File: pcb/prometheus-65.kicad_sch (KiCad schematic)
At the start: 0 parts

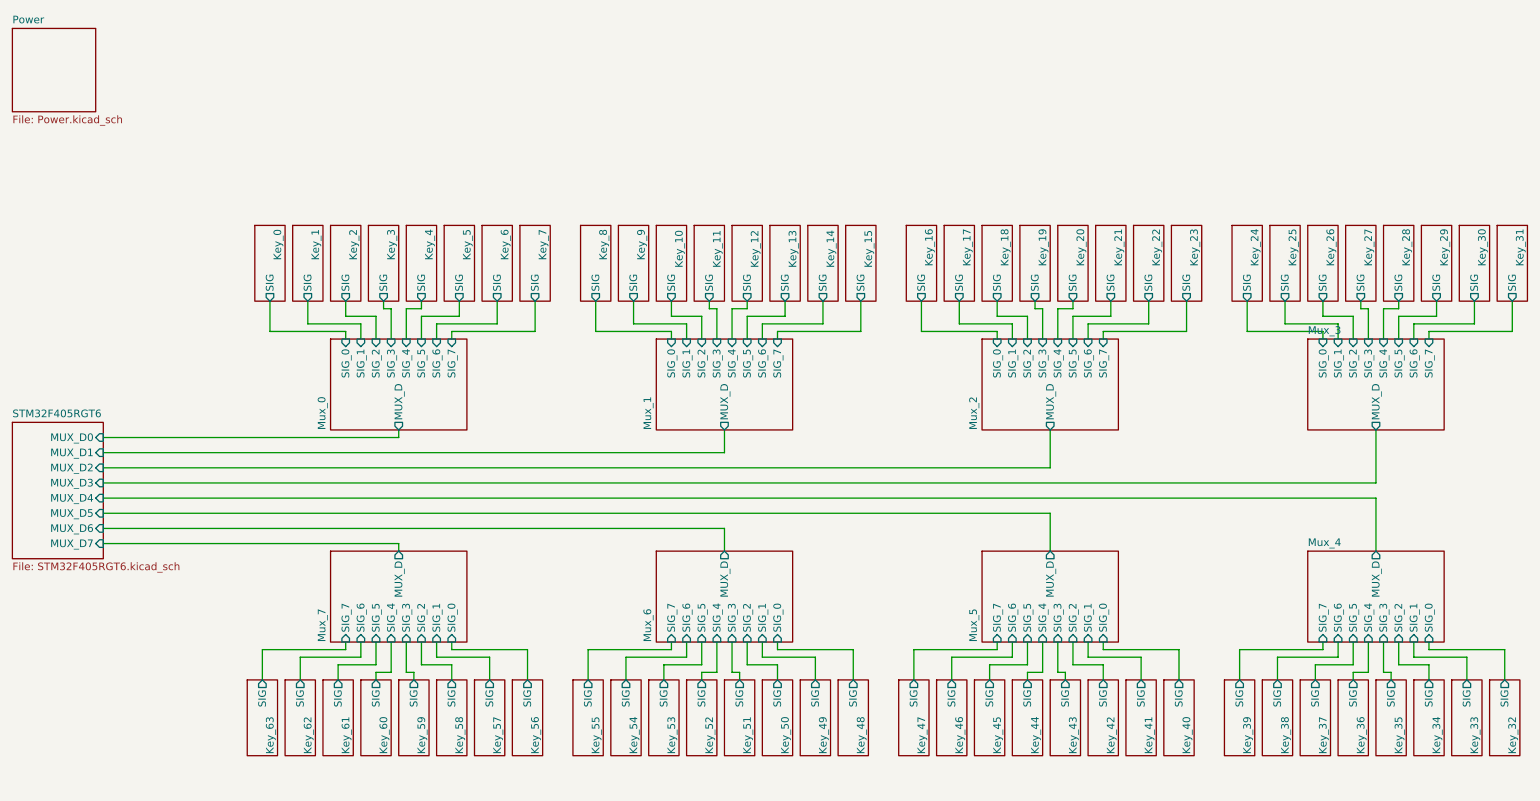
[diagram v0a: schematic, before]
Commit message: feat: added the rotary encoder
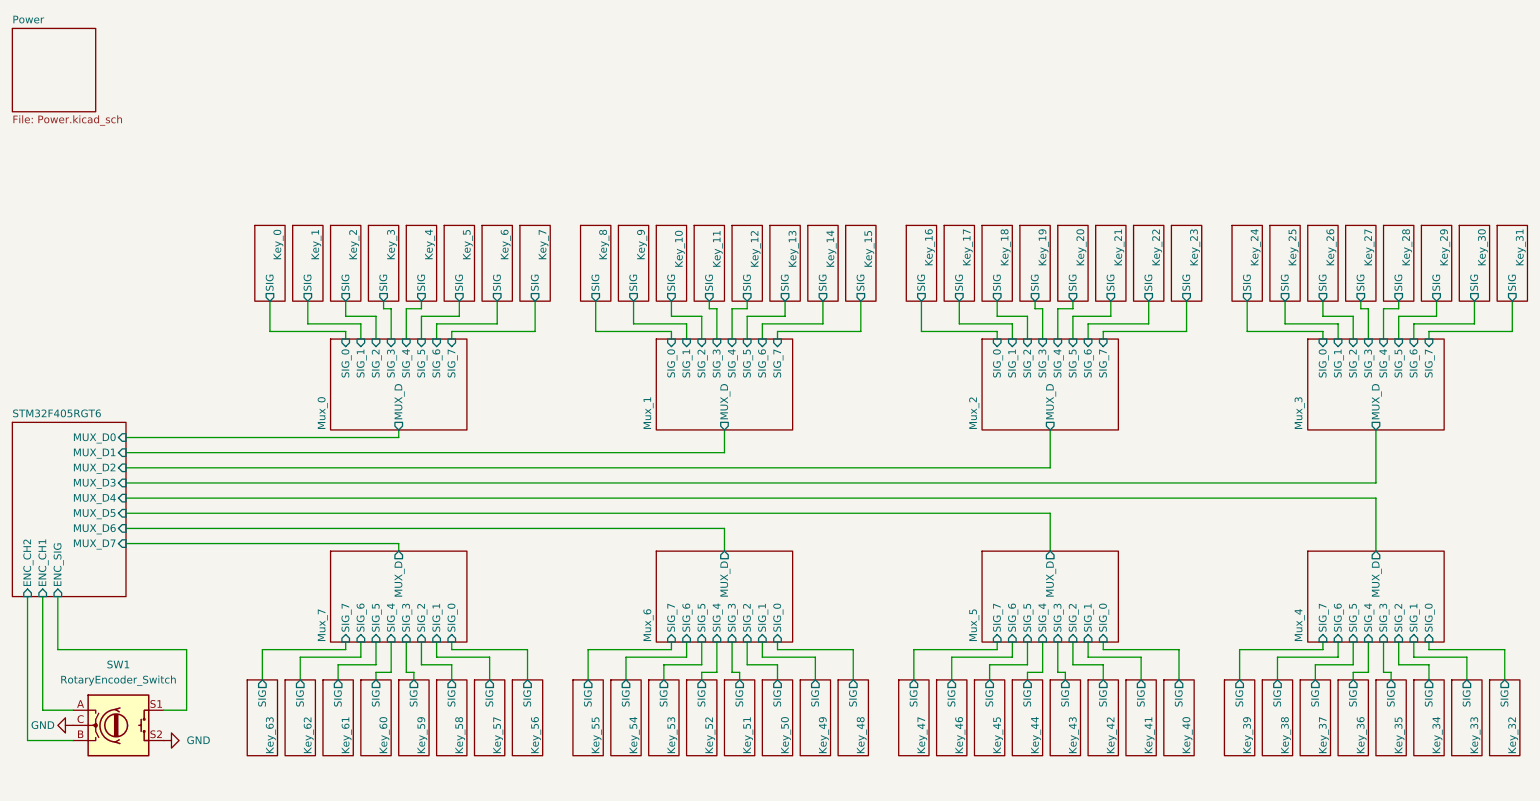
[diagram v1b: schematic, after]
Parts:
- added SW1: RotaryEncoder_Switch, symbol Device:RotaryEncoder_Switch
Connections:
- new net GND: SW1.C, SW1.S2
- new net STM32F405RGT6/ENC_CH1: SW1.A
- new net STM32F405RGT6/ENC_CH2: SW1.B
- new net STM32F405RGT6/ENC_SIG: SW1.S1
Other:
- sheet STM32F405RGT6 ports: added ENC_CH1, ENC_CH2, ENC_SIG; removed none

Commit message: feat: added LED circuit and wired to STM32
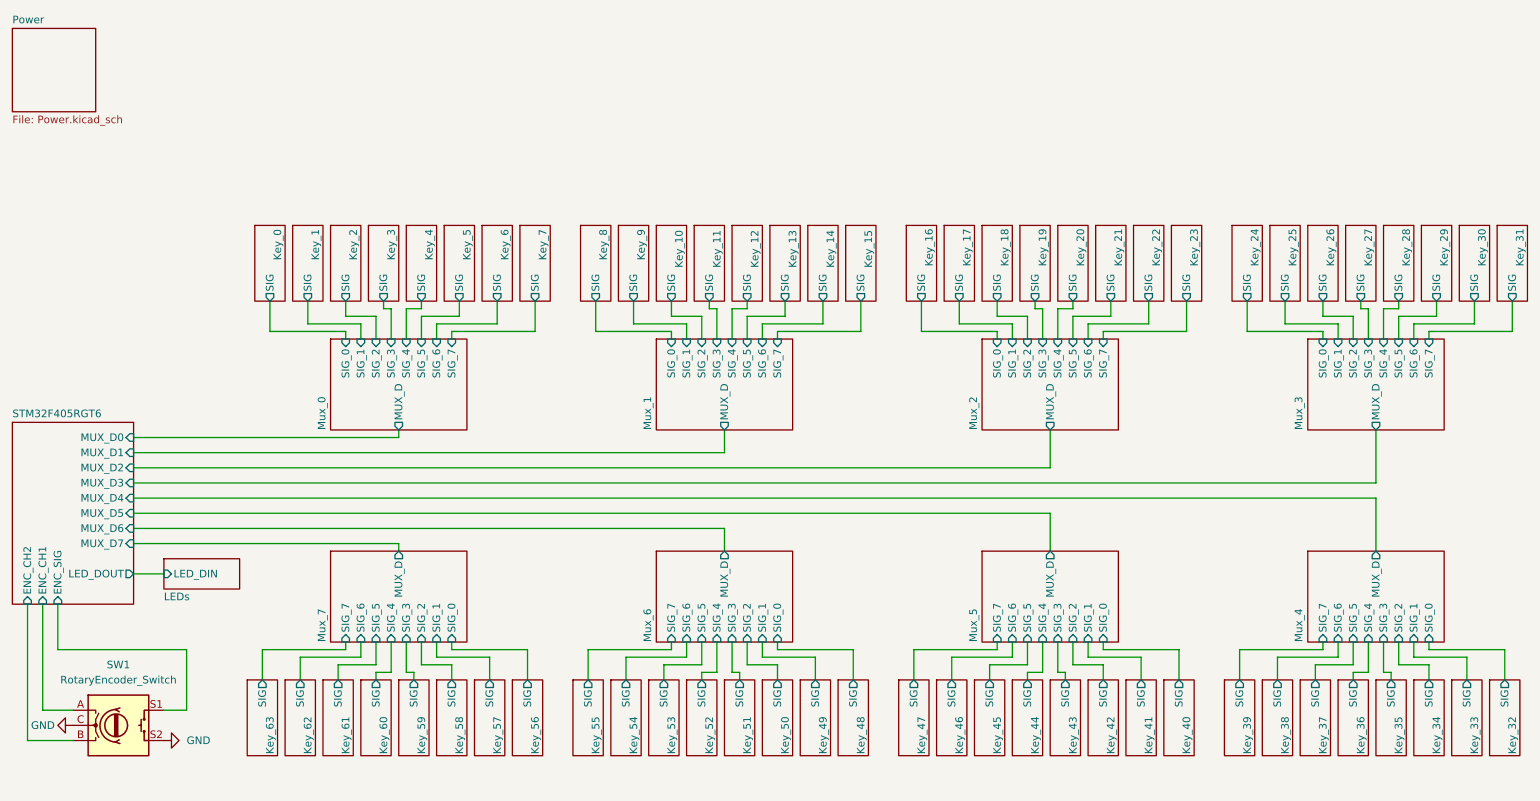
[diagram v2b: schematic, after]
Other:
- added sheet LEDs (LEDs.kicad_sch)
- sheet STM32F405RGT6 ports: added LED_DOUT; removed none

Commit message: feat: assigned footprints for each symbol and switch
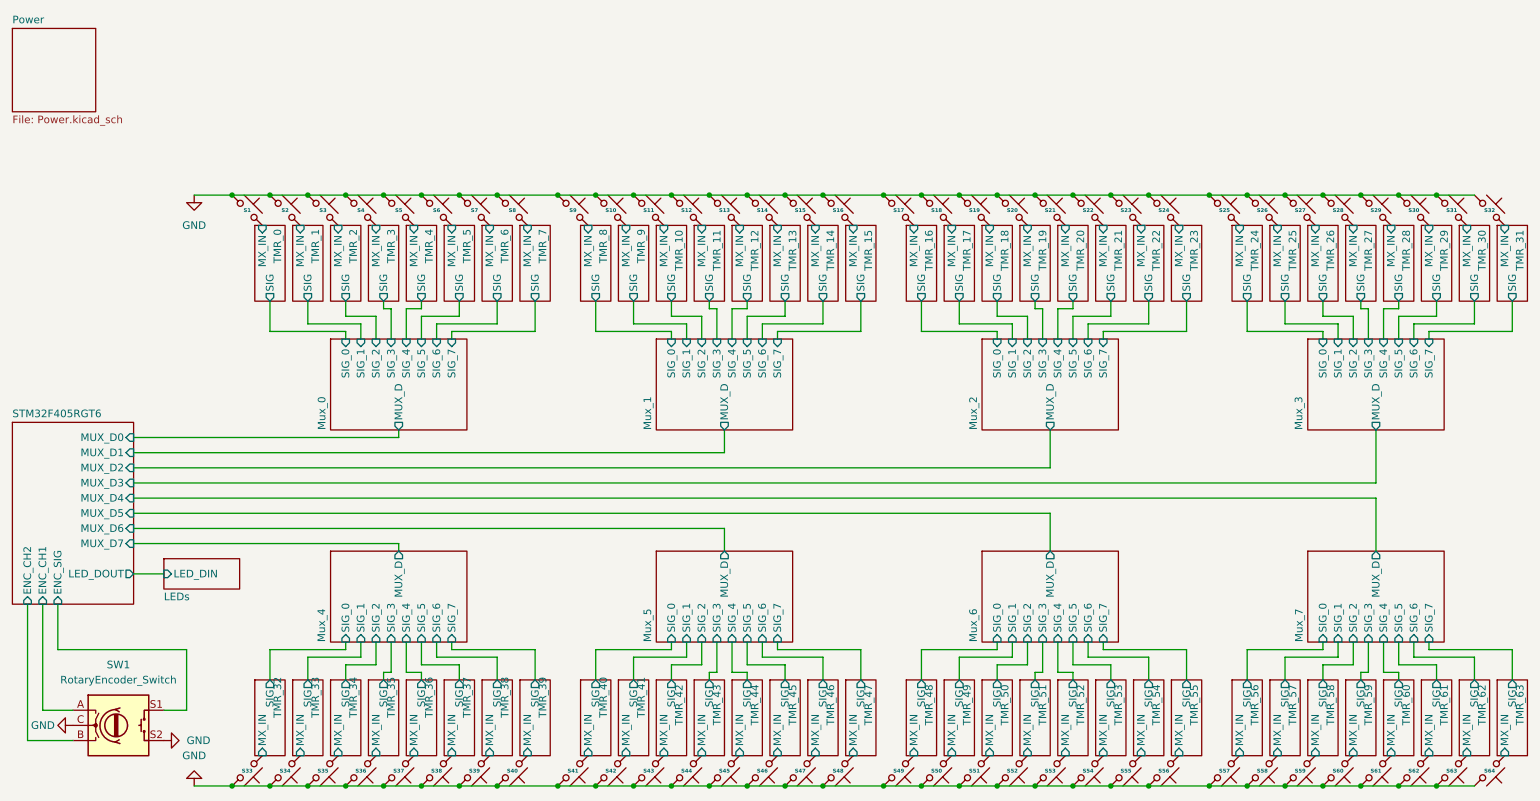
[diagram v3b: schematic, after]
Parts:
- added S1, S10, S12, S13, S17, S18, S19, S2, S20, S21, S22, S23, S24, S25, S26, S27, S28, S29, S3, S30, S31, S33, S34, S35, S36, S37, S38, S39, S4, S40, S41, S42, S43, S44, S45, S46, S47, S49, S50, S51, S53, S54, S55, S58, S6, S60, S64, S7, S9: ~, ScottoKeebs_Hotswap:Hotswap_MX_Plated_1.00u, symbol ScottoKeebs:Placeholder_Keyswitch
- added S11, S57: ~, ScottoKeebs_Hotswap:Hotswap_MX_Plated_2.25u, symbol ScottoKeebs:Placeholder_Keyswitch
- added S14, S15, S16, S48, S61, S62, S63: ~, ScottoKeebs_Hotswap:Hotswap_MX_Plated_1.25u, symbol ScottoKeebs:Placeholder_Keyswitch
- added S32: ~, ScottoKeebs_Hotswap:Hotswap_MX_Plated_6.25u, symbol ScottoKeebs:Placeholder_Keyswitch
- added S5, S56: ~, ScottoKeebs_Hotswap:Hotswap_MX_Plated_1.50u, symbol ScottoKeebs:Placeholder_Keyswitch
- added S52: ~, ScottoKeebs_Hotswap:Hotswap_MX_Plated_2.00u, symbol ScottoKeebs:Placeholder_Keyswitch
- added S59: ~, ScottoKeebs_Hotswap:Hotswap_MX_Plated_2.75u, symbol ScottoKeebs:Placeholder_Keyswitch
- added S8: ~, ScottoKeebs_Hotswap:Hotswap_MX_Plated_1.75u, symbol ScottoKeebs:Placeholder_Keyswitch
- SW1: footprint (none) -> Rotary_Encoder:RotaryEncoder_Alps_EC11E-Switch_Vertical_H20mm
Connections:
- net GND: now also S1.1, S10.1, S11.1, S12.1, S13.1, S14.1, S15.1, S16.1, S17.1, S18.1, S19.1, S2.1, S20.1, S21.1, S22.1, S23.1, S24.1, S25.1, S26.1, S27.1, S28.1, S29.1, S3.1, S30.1, S31.1, S32.1, S33.1, S34.1, S35.1, S36.1, S37.1, S38.1, S39.1, S4.1, S40.1, S41.1, S42.1, S43.1, S44.1, S45.1, S46.1, S47.1, S48.1, S49.1, S5.1, S50.1, S51.1, S52.1, S53.1, S54.1, S55.1, S56.1, S57.1, S58.1, S59.1, S6.1, S60.1, S61.1, S62.1, S63.1, S64.1, S7.1, S8.1, S9.1
- new net TMR_0/MX_IN: S1.2
- new net TMR_1/MX_IN: S2.2
- new net TMR_10/MX_IN: S11.2
- new net TMR_11/MX_IN: S12.2
- new net TMR_12/MX_IN: S13.2
- new net TMR_13/MX_IN: S14.2
- new net TMR_14/MX_IN: S15.2
- new net TMR_15/MX_IN: S16.2
- new net TMR_16/MX_IN: S17.2
- new net TMR_17/MX_IN: S18.2
- new net TMR_18/MX_IN: S19.2
- new net TMR_19/MX_IN: S20.2
- new net TMR_2/MX_IN: S3.2
- new net TMR_20/MX_IN: S21.2
- new net TMR_21/MX_IN: S22.2
- new net TMR_22/MX_IN: S23.2
- new net TMR_23/MX_IN: S24.2
- new net TMR_24/MX_IN: S25.2
- new net TMR_25/MX_IN: S26.2
- new net TMR_26/MX_IN: S27.2
- new net TMR_27/MX_IN: S28.2
- new net TMR_28/MX_IN: S29.2
- new net TMR_29/MX_IN: S30.2
- new net TMR_3/MX_IN: S4.2
- new net TMR_30/MX_IN: S31.2
- new net TMR_31/MX_IN: S32.2
- new net TMR_32/MX_IN: S33.2
- new net TMR_33/MX_IN: S34.2
- new net TMR_34/MX_IN: S35.2
- new net TMR_35/MX_IN: S36.2
- new net TMR_36/MX_IN: S37.2
- new net TMR_37/MX_IN: S38.2
- new net TMR_38/MX_IN: S39.2
- new net TMR_39/MX_IN: S40.2
- new net TMR_4/MX_IN: S5.2
- new net TMR_40/MX_IN: S41.2
- new net TMR_41/MX_IN: S42.2
- new net TMR_42/MX_IN: S43.2
- new net TMR_43/MX_IN: S44.2
- new net TMR_44/MX_IN: S45.2
- new net TMR_45/MX_IN: S46.2
- new net TMR_46/MX_IN: S47.2
- new net TMR_47/MX_IN: S48.2
- new net TMR_48/MX_IN: S49.2
- new net TMR_49/MX_IN: S50.2
- new net TMR_5/MX_IN: S6.2
- new net TMR_50/MX_IN: S51.2
- new net TMR_51/MX_IN: S52.2
- new net TMR_52/MX_IN: S53.2
- new net TMR_53/MX_IN: S54.2
- new net TMR_54/MX_IN: S55.2
- new net TMR_55/MX_IN: S56.2
- new net TMR_56/MX_IN: S57.2
- new net TMR_57/MX_IN: S58.2
- new net TMR_58/MX_IN: S59.2
- new net TMR_59/MX_IN: S60.2
- new net TMR_6/MX_IN: S7.2
- new net TMR_60/MX_IN: S61.2
- new net TMR_61/MX_IN: S62.2
- new net TMR_62/MX_IN: S63.2
- new net TMR_63/MX_IN: S64.2
- new net TMR_7/MX_IN: S8.2
- new net TMR_8/MX_IN: S9.2
- new net TMR_9/MX_IN: S10.2
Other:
- sheet Key_0 renamed TMR_0
- removed sheet Key_1
- removed sheet Key_10
- removed sheet Key_11
- removed sheet Key_12
- removed sheet Key_13
- removed sheet Key_14
- removed sheet Key_15
- removed sheet Key_16
- removed sheet Key_17
- removed sheet Key_18
- removed sheet Key_19
- removed sheet Key_2
- removed sheet Key_20
- removed sheet Key_21
- removed sheet Key_22
- removed sheet Key_23
- removed sheet Key_24
- removed sheet Key_25
- removed sheet Key_26
- removed sheet Key_27
- removed sheet Key_28
- removed sheet Key_29
- removed sheet Key_3
- removed sheet Key_30
- removed sheet Key_31
- removed sheet Key_32
- removed sheet Key_33
- removed sheet Key_34
- removed sheet Key_35
- removed sheet Key_36
- removed sheet Key_37
- removed sheet Key_38
- removed sheet Key_39
- removed sheet Key_4
- removed sheet Key_40
- removed sheet Key_41
- removed sheet Key_42
- removed sheet Key_43
- removed sheet Key_44
- removed sheet Key_45
- removed sheet Key_46
- removed sheet Key_47
- removed sheet Key_48
- removed sheet Key_49
- removed sheet Key_5
- removed sheet Key_50
- removed sheet Key_51
- removed sheet Key_52
- removed sheet Key_53
- removed sheet Key_54
- removed sheet Key_55
- removed sheet Key_56
- removed sheet Key_57
- removed sheet Key_58
- removed sheet Key_59
- removed sheet Key_6
- removed sheet Key_60
- removed sheet Key_61
- removed sheet Key_62
- removed sheet Key_63
- removed sheet Key_7
- removed sheet Key_8
- removed sheet Key_9
- added sheet TMR_1 (TMR.kicad_sch)
- added sheet TMR_10 (TMR.kicad_sch)
- added sheet TMR_11 (TMR.kicad_sch)
- added sheet TMR_12 (TMR.kicad_sch)
- added sheet TMR_13 (TMR.kicad_sch)
- added sheet TMR_14 (TMR.kicad_sch)
- added sheet TMR_15 (TMR.kicad_sch)
- added sheet TMR_16 (TMR.kicad_sch)
- added sheet TMR_17 (TMR.kicad_sch)
- added sheet TMR_18 (TMR.kicad_sch)
- added sheet TMR_19 (TMR.kicad_sch)
- added sheet TMR_2 (TMR.kicad_sch)
- added sheet TMR_20 (TMR.kicad_sch)
- added sheet TMR_21 (TMR.kicad_sch)
- added sheet TMR_22 (TMR.kicad_sch)
- added sheet TMR_23 (TMR.kicad_sch)
- added sheet TMR_24 (TMR.kicad_sch)
- added sheet TMR_25 (TMR.kicad_sch)
- added sheet TMR_26 (TMR.kicad_sch)
- added sheet TMR_27 (TMR.kicad_sch)
- added sheet TMR_28 (TMR.kicad_sch)
- added sheet TMR_29 (TMR.kicad_sch)
- added sheet TMR_3 (TMR.kicad_sch)
- added sheet TMR_30 (TMR.kicad_sch)
- added sheet TMR_31 (TMR.kicad_sch)
- added sheet TMR_32 (TMR.kicad_sch)
- added sheet TMR_33 (TMR.kicad_sch)
- added sheet TMR_34 (TMR.kicad_sch)
- added sheet TMR_35 (TMR.kicad_sch)
- added sheet TMR_36 (TMR.kicad_sch)
- added sheet TMR_37 (TMR.kicad_sch)
- added sheet TMR_38 (TMR.kicad_sch)
- added sheet TMR_39 (TMR.kicad_sch)
- added sheet TMR_4 (TMR.kicad_sch)
- added sheet TMR_40 (TMR.kicad_sch)
- added sheet TMR_41 (TMR.kicad_sch)
- added sheet TMR_42 (TMR.kicad_sch)
- added sheet TMR_43 (TMR.kicad_sch)
- added sheet TMR_44 (TMR.kicad_sch)
- added sheet TMR_45 (TMR.kicad_sch)
- added sheet TMR_46 (TMR.kicad_sch)
- added sheet TMR_47 (TMR.kicad_sch)
- added sheet TMR_48 (TMR.kicad_sch)
- added sheet TMR_49 (TMR.kicad_sch)
- added sheet TMR_5 (TMR.kicad_sch)
- added sheet TMR_50 (TMR.kicad_sch)
- added sheet TMR_51 (TMR.kicad_sch)
- added sheet TMR_52 (TMR.kicad_sch)
- added sheet TMR_53 (TMR.kicad_sch)
- added sheet TMR_54 (TMR.kicad_sch)
- added sheet TMR_55 (TMR.kicad_sch)
- added sheet TMR_56 (TMR.kicad_sch)
- added sheet TMR_57 (TMR.kicad_sch)
- added sheet TMR_58 (TMR.kicad_sch)
- added sheet TMR_59 (TMR.kicad_sch)
- added sheet TMR_6 (TMR.kicad_sch)
- added sheet TMR_60 (TMR.kicad_sch)
- added sheet TMR_61 (TMR.kicad_sch)
- added sheet TMR_62 (TMR.kicad_sch)
- added sheet TMR_63 (TMR.kicad_sch)
- added sheet TMR_7 (TMR.kicad_sch)
- added sheet TMR_8 (TMR.kicad_sch)
- added sheet TMR_9 (TMR.kicad_sch)
- sheet TMR_0: file Key.kicad_sch -> TMR.kicad_sch
- sheet TMR_0 ports: added MX_IN; removed none
